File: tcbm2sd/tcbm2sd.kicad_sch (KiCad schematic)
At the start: 27 parts, among them J1 TCBM, J2 JTAG, J4 AMS1117, J5 SD CARD, J7 ALT_A6_A7, SW1 BUT_PREV, SW2 BUT_NEXT, U1 XC9572XL-VQ64, U2 Arduino Pro Mini, U3 AMS1117-3.3, U4 27C512

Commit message: updated routing
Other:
- note added: "A7 shorted to GND at RESET = disable buttons (A6 won't be checked) else: A6 shorted to GND at RESET = disable Arduino A6 shorted to GND at RESET = enable TCBM conn (A6 can be shorted by TCBM cable or by holding SW1) SW1/SW2 option for next/previous disk image (autolist)"
- note removed: "A6 shorted to GND at RESET = disable Arduino A6 shorted to GND at RESET = enable TCBM conn (A6 can be shorted by TCBM cable or by holding SW1) SW1/SW2 option for next/previous disk image (autolist)"
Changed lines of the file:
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@@
     (effects (font (size 1.27 1.27)) (justify left bottom))
   )
-  (text "A6 shorted to GND at RESET = disable Arduino\nA6 shorted to GND at RESET = enable TCBM conn\n(A6 can be shorted by TCBM cable or by holding SW1)\nSW1/SW2 option for next/previous disk image (autolist)"
-    (at 196.85 154.305 0)
+  (text "A7 shorted to GND at RESET = disable buttons (A6 won't be checked)\nelse:\nA6 shorted to GND at RESET = disable Arduino\nA6 shorted to GND at RESET = enable TCBM conn\n(A6 can be shorted by TCBM cable or by holding SW1)\nSW1/SW2 option for next/previous disk image (autolist)"
+    (at 184.785 161.925 0)
     (effects (font (size 1.27 1.27)) (justify left bottom))
   )

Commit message: dual footprint for pushbutton switch straight or angled
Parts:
- SW1, SW2: footprint Button_Switch_THT:SW_PUSH_6mm -> LittleSixteen:SW_PUSH_6mm_OR_SW_Tactile_SPST_Angled_PTS645Vx58-2LFS
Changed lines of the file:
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@@
     (property "Reference" "SW2" (id 0) (at 229.235 120.65 0))
     (property "Value" "BUT_NEXT" (id 1) (at 229.235 123.19 0))
-    (property "Footprint" "Button_Switch_THT:SW_PUSH_6mm" (id 2) (at 229.235 123.19 0)
+    (property "Footprint" "LittleSixteen:SW_PUSH_6mm_OR_SW_Tactile_SPST_Angled_PTS645Vx58-2LFS" (id 2) (at 229.235 123.19 0)
       (effects (font (size 1.27 1.27)) hide)
     )
@@
     (property "Reference" "SW1" (id 0) (at 229.235 110.49 0))
     (property "Value" "BUT_PREV" (id 1) (at 229.235 113.03 0))
-    (property "Footprint" "Button_Switch_THT:SW_PUSH_6mm" (id 2) (at 229.235 113.03 0)
+    (property "Footprint" "LittleSixteen:SW_PUSH_6mm_OR_SW_Tactile_SPST_Angled_PTS645Vx58-2LFS" (id 2) (at 229.235 113.03 0)
       (effects (font (size 1.27 1.27)) hide)
     )
@@
     )
     (path "/c959f069-2b8c-4c54-a835-a0cd1e70cff6"
-      (reference "SW1") (unit 1) (value "BUT_PREV") (footprint "Button_Switch_THT:SW_PUSH_6mm")
+      (reference "SW1") (unit 1) (value "BUT_PREV") (footprint "LittleSixteen:SW_PUSH_6mm_OR_SW_Tactile_SPST_Angled_PTS645Vx58-2LFS")
     )
     (path "/9077d6af-aba8-40fe-9d96-a7e025a21e36"
-      (reference "SW2") (unit 1) (value "BUT_NEXT") (footprint "Button_Switch_THT:SW_PUSH_6mm")
+      (reference "SW2") (unit 1) (value "BUT_NEXT") (footprint "LittleSixteen:SW_PUSH_6mm_OR_SW_Tactile_SPST_Angled_PTS645Vx58-2LFS")
     )
     (path "/71fe6854-21dc-4774-adbd-eb6f5e8f643d"

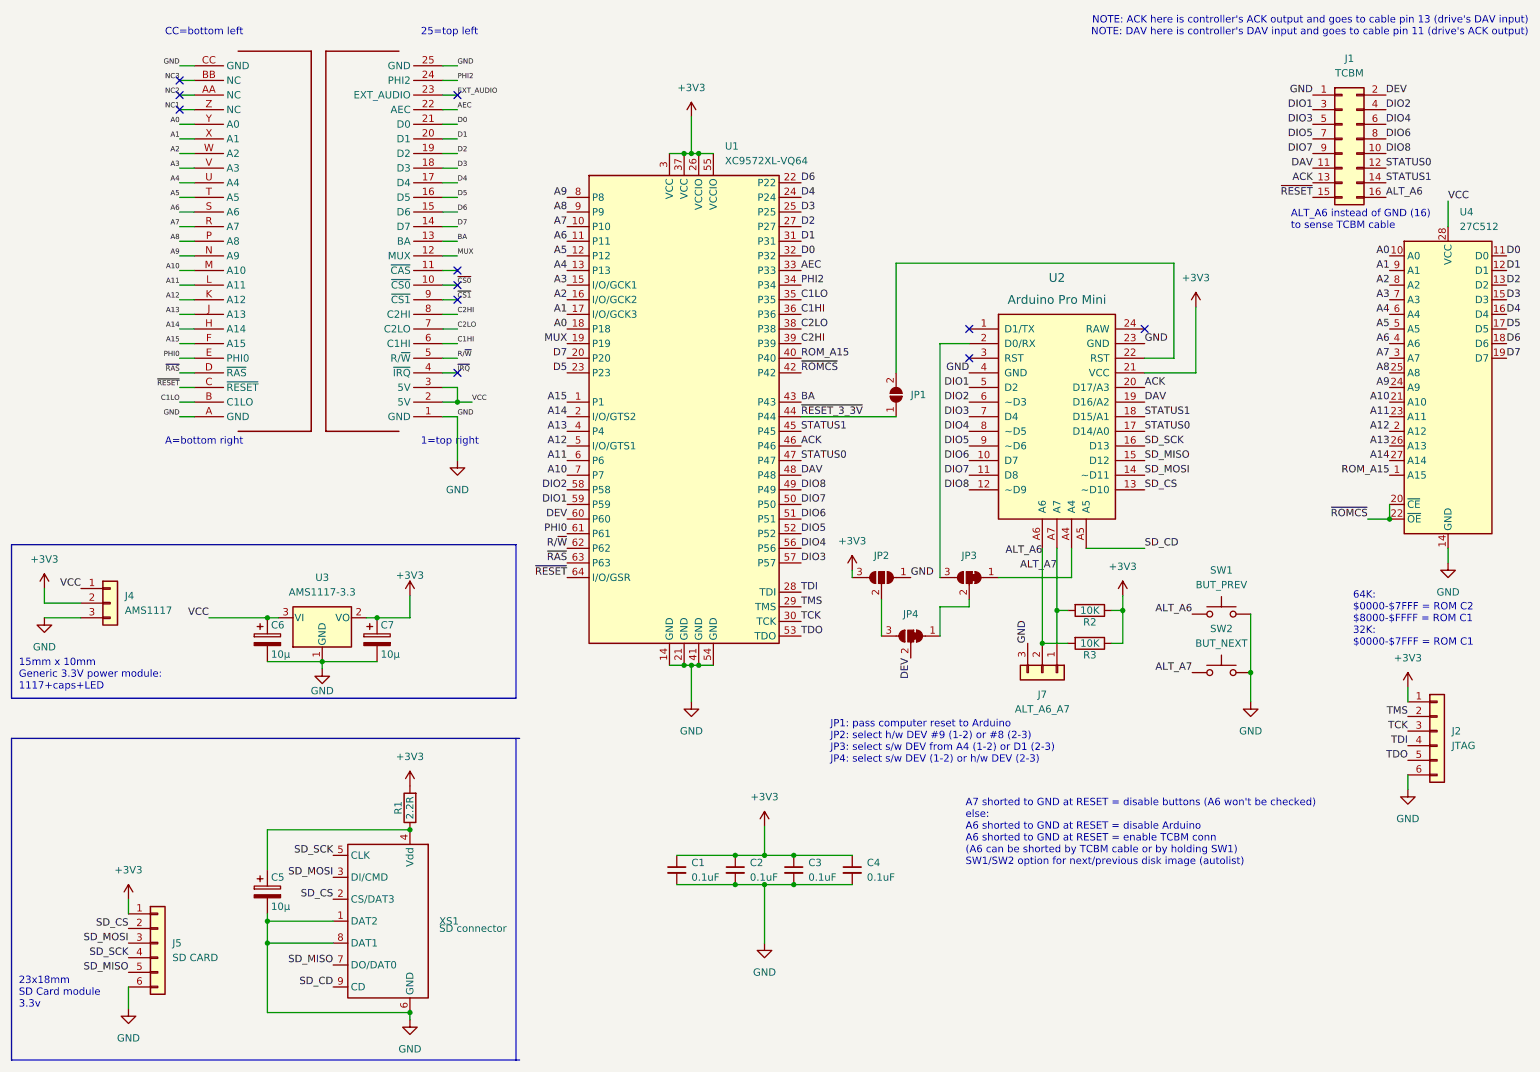
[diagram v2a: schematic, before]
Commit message: v1.4 with correct silkscreen info about C1/C2 ROM banks and 3.3V /RESET routed to TCBM connector instead of 5V /RESET
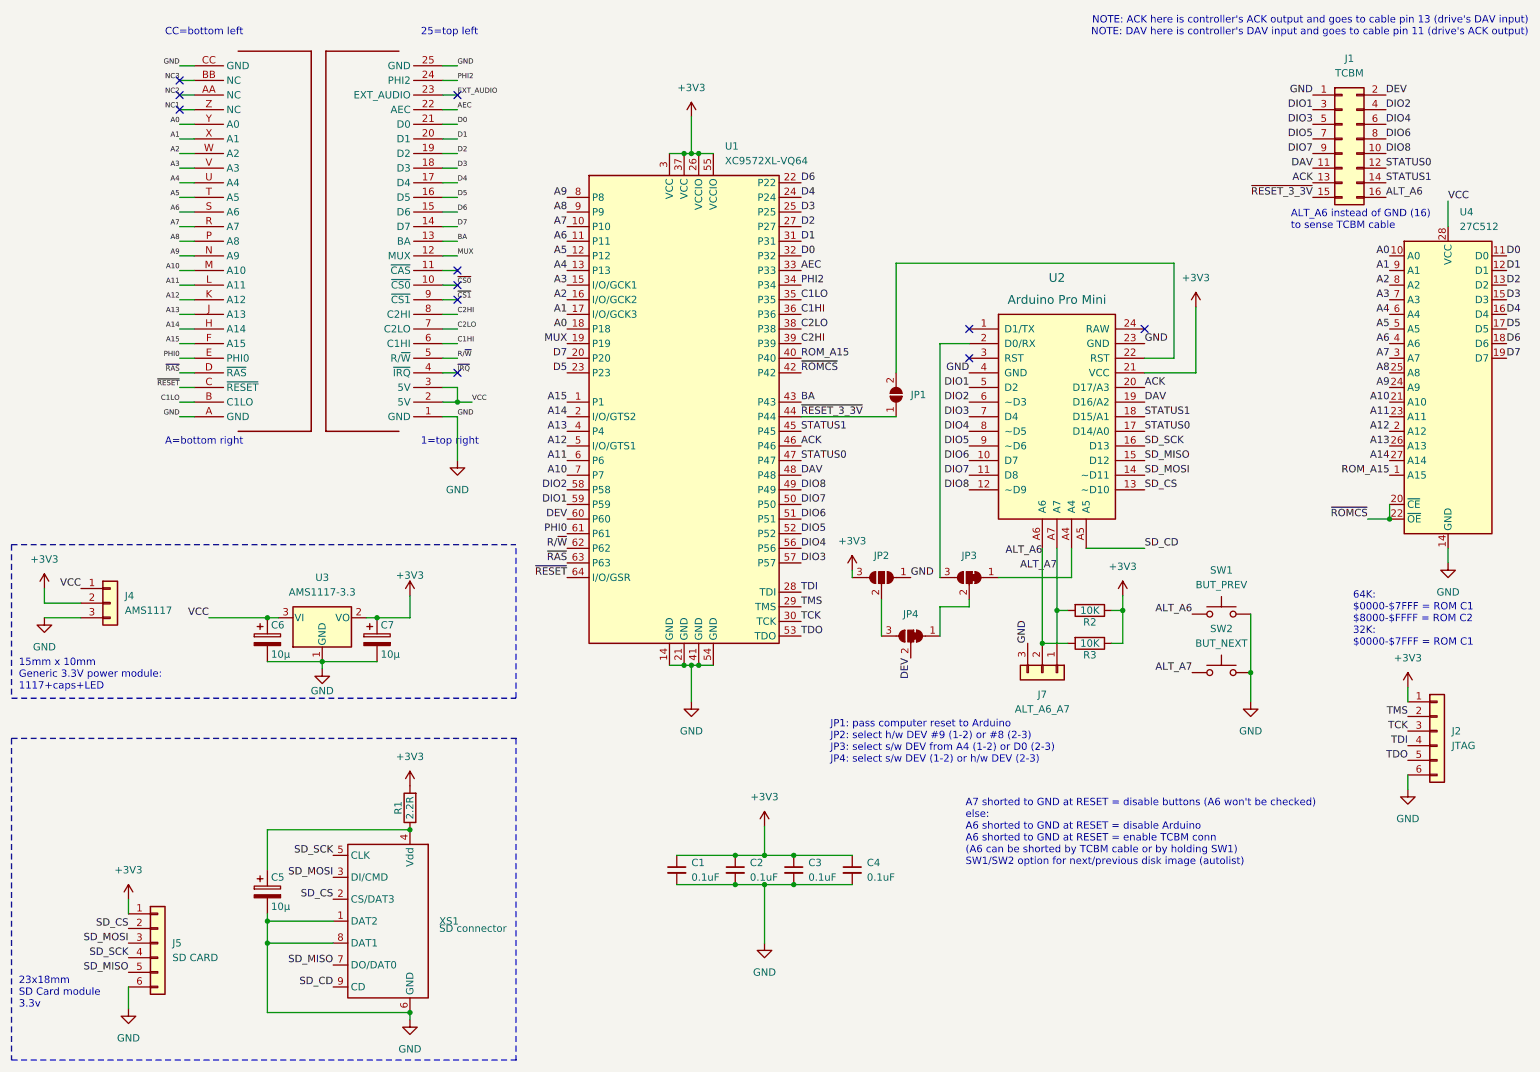
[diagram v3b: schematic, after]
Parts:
- C5, C6, C7: footprint Capacitor_Tantalum_SMD:CP_EIA-3216-12_Kemet-S_Pad1.58x1.35mm_HandSolder -> Capacitor_Tantalum_SMD:CP_EIA-3216-12_Kemet-S_HandSolder
- XS1: symbol uSD_push-push_ebay:SD_ebay-uSD-push/push_SMD -> uSD_push-push_ebay:SD_ebay-uSD-push/push_SMD
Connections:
- net ~{RESET_3_3V}: now also J1.15 (Pin_15)
- net ~{RESET}: no longer J1.15 (Pin_15)
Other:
- note added: "64K: $0000-$7FFF = ROM C1 $8000-$FFFF = ROM C2 32K: $0000-$7FFF = ROM C1"
- note added: "JP1: pass computer reset to Arduino JP2: select h/w DEV #9 (1-2) or #8 (2-3) JP3: select s/w DEV from A4 (1-2) or D0 (2-3) JP4: select s/w DEV (1-2) or h/w DEV (2-3)"
- note removed: "64K: $0000-$7FFF = ROM C2 $8000-$FFFF = ROM C1 32K: $0000-$7FFF = ROM C1"
- note removed: "JP1: pass computer reset to Arduino JP2: select h/w DEV #9 (1-2) or #8 (2-3) JP3: select s/w DEV from A4 (1-2) or D1 (2-3) JP4: select s/w DEV (1-2) or h/w DEV (2-3)"
